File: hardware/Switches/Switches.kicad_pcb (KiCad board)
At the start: 4 copper layers, 120 x 75 mm, 107 parts, among them J101 BusBar, J102 BusBar, J103 BusBar, J104 BusBar, J105 Conn_02x03_Odd_Even, Q101 IPT015N10N5, Q102 IPT015N10N5, Q103 IPT015N10N5, Q104 IPT015N10N5, Q105 IPT015N10N5, Q106 IPT015N10N5, Q107 IPT015N10N5, Q108 IPT015N10N5, Q109 IPT015N10N5, Q110 IPT015N10N5, Q111 IPT015N10N5, Q112 IPT015N10N5, U101 UCC27211DDAR, U102 UCC27211DDAR

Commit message: silkscreen and export gerbers
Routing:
- net (no net): track 1.21 -> 0.00 mm, vias 1 -> 0
- net GND: vias 1067 -> 1032
- net +BATT: vias 1033 -> 1013
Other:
- board text added: "+15 +15 +15 +15 +15 PWM_L1 PWM_H1 PWM_L2 PWM_H2 +5VA"
- board text added: "+VBAT"
- board text added: "DRIVER_1"
- board text added: "DRIVER_2"
- board text added: "GND"
- board text added: "GND GND GND GND GND SL1 SL2 Vin Temp GNDA"
- board text added: "SL1"
- board text added: "SL1 HIGH"
- board text added: "SL1 LOW"
- board text added: "SL2"
- board text added: "SL2 HIGH"
- board text added: "SL2 LOW"
- board text added: "SNUBBER +VBAT/SL1"
- board text added: "SNUBBER +VBAT/SL2"
- board text added: "SNUBBER SL1/GND"
- board text added: "SNUBBER SL2/GND"
- board text added: "TEMP"
- board text added: "Vin"

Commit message: Gerbers re-generated with JCLJCLJLC.. string
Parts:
- added REF**: OSHW-Logo2_9.8x8mm_SilkScreen, Symbol:OSHW-Logo2_9.8x8mm_SilkScreen, F.Cu at (159.2, 116.4)
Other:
- board text added: "Designed by Zênite Solar Boat Team - github.com/ZeniteSolar"
- board text added: "JLCJLCJLCJLC"

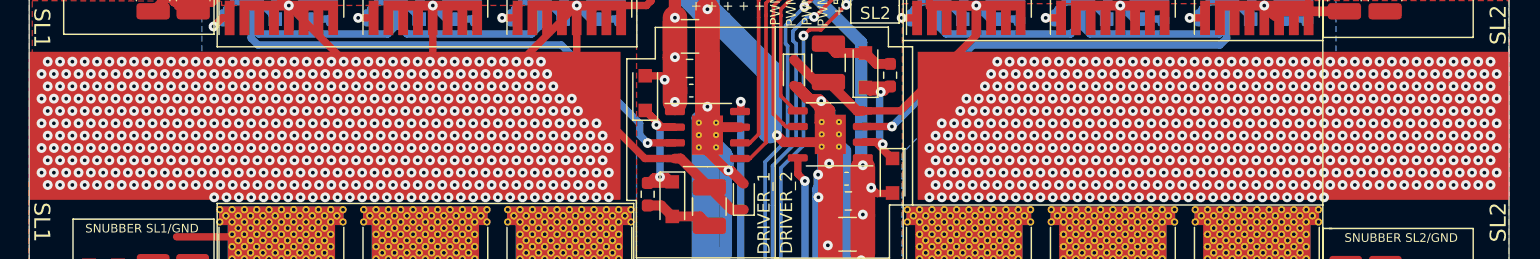
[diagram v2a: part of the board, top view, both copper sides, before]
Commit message: Add more holes to better pull the heatsink
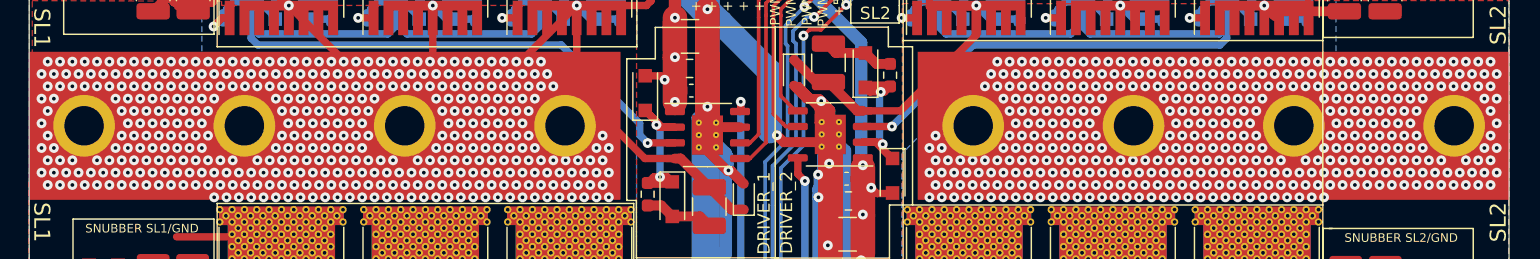
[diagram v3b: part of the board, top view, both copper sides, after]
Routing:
- net /SL1: track 126.9 -> 125.2 mm, vias 527 -> 426
- net /SL2: vias 527 -> 431
- net (no net): vias 0 -> 2

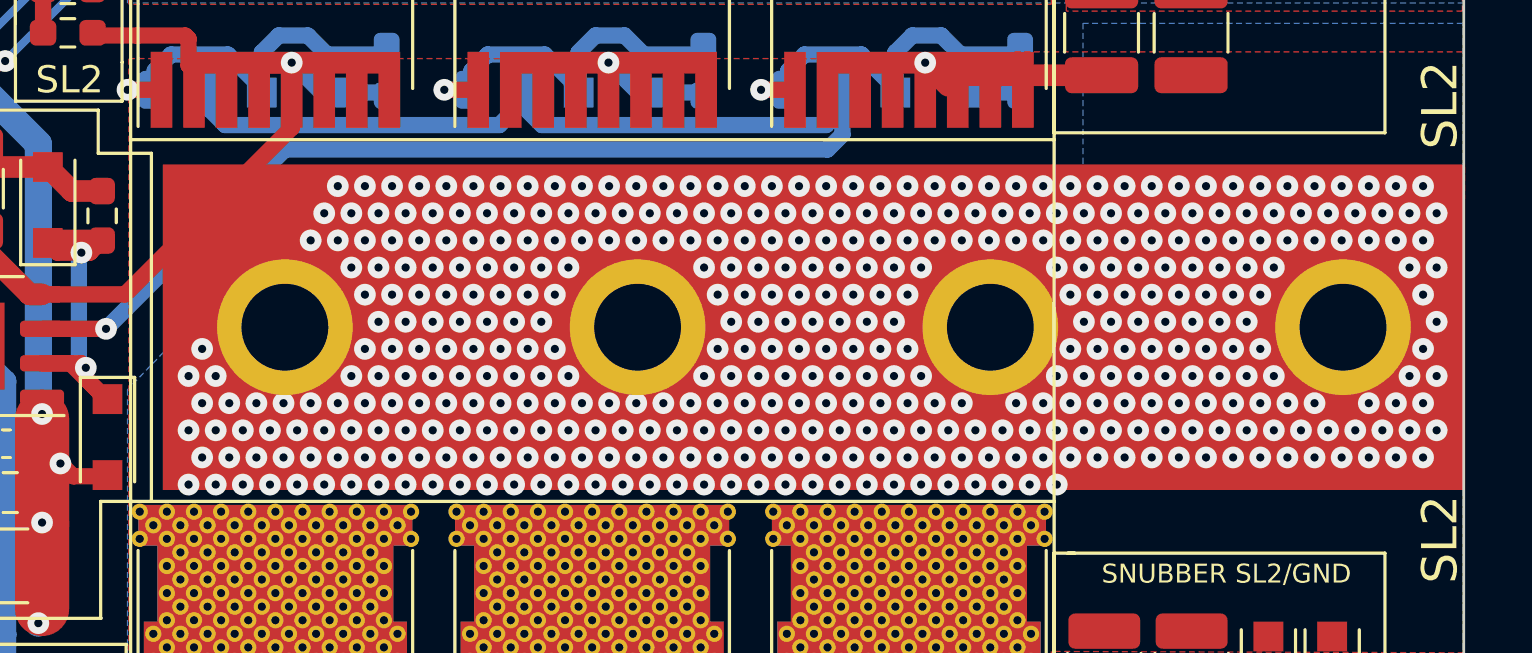
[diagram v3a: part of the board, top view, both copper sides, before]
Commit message: Remove the solder mask from heatsink region
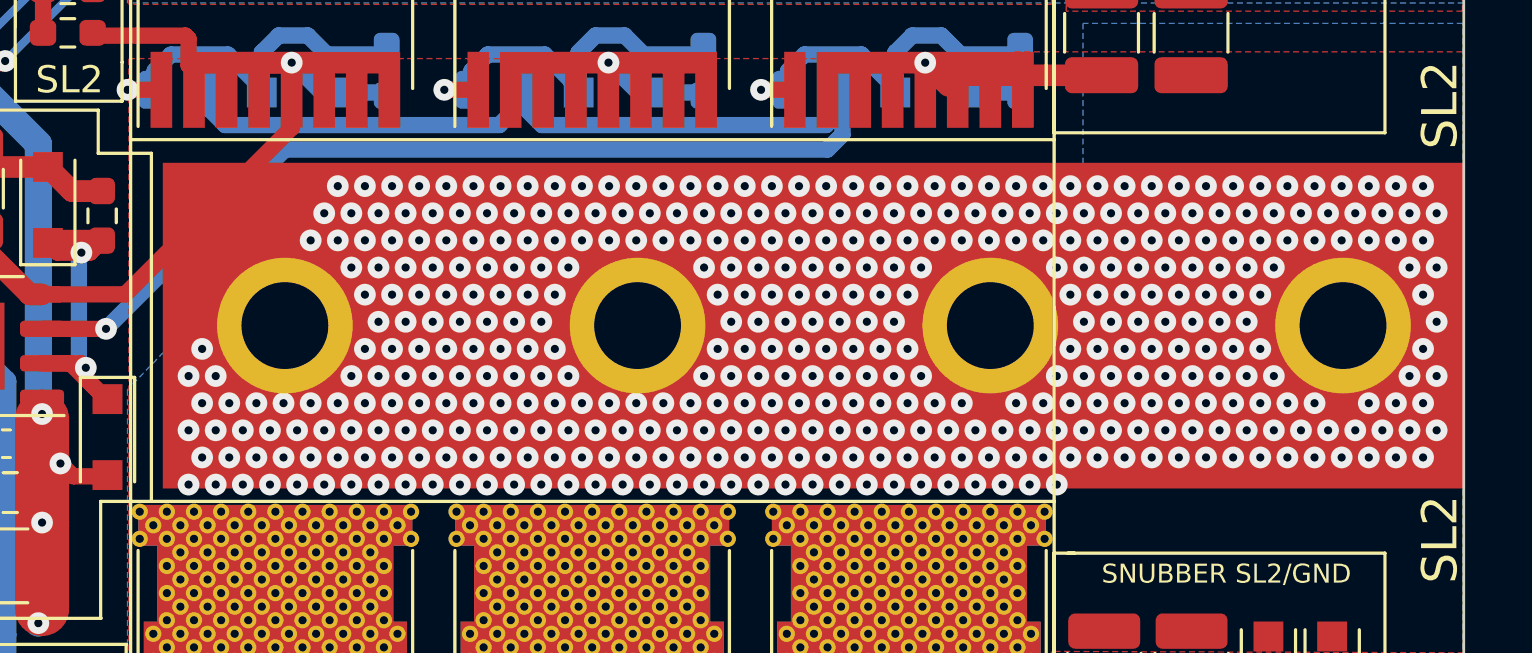
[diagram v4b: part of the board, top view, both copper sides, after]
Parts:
- moved J104 0.06 mm to (198.3, 100.4)
